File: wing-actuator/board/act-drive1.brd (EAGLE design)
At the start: 112.5 x 79.2 mm, 137 parts, among them J1 POWER_JACKPTH_LOCK, Q1 BSS123, Q2 BSS123, Q3 BSS123, Q4 BSS123, Q5 BSS123, Q6 BSS123, T1 ATB3225, U1 LT3468-1, X1 SMA-142-0701-801/806, X2 SMA-142-0701-801/806, X3 SMA-142-0701-801/806, X4 SMA-142-0701-801/806, X5 2516-, X6 2516-, X7 SSW-102-02-S-D

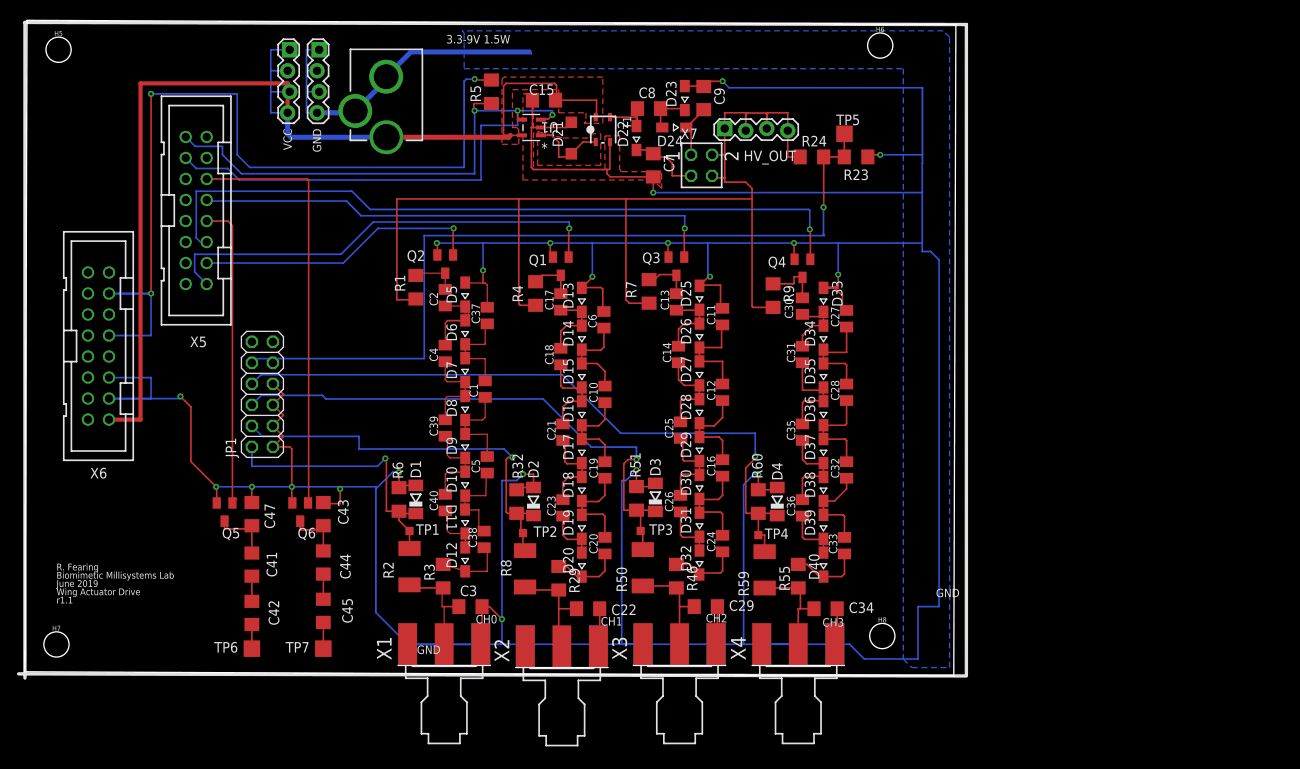
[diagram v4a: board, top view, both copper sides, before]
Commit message: done routing. need to add attributes for BoM
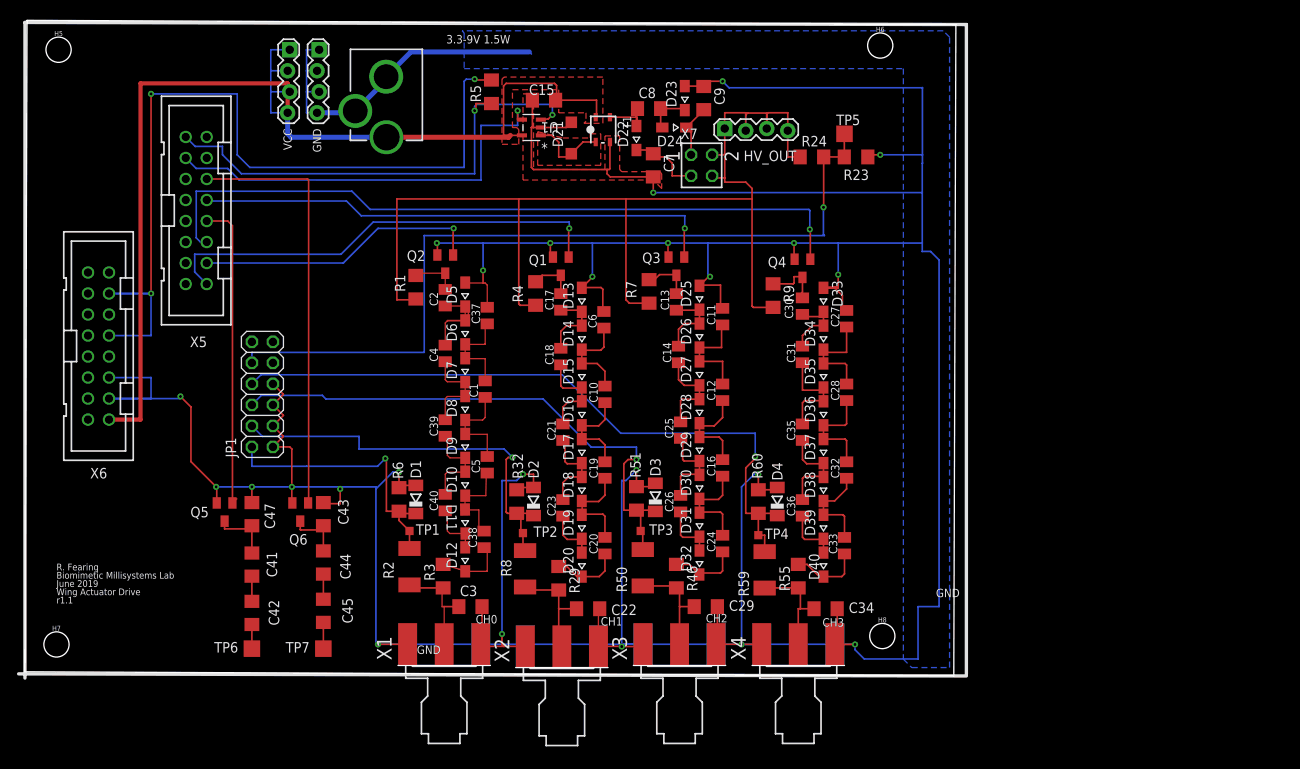
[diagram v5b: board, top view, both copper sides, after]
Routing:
- net GND: track 617.0 -> 639.0 mm, vias 21 -> 25
- net DONE*: track 59.5 -> 60.7 mm

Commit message: renumbered parts
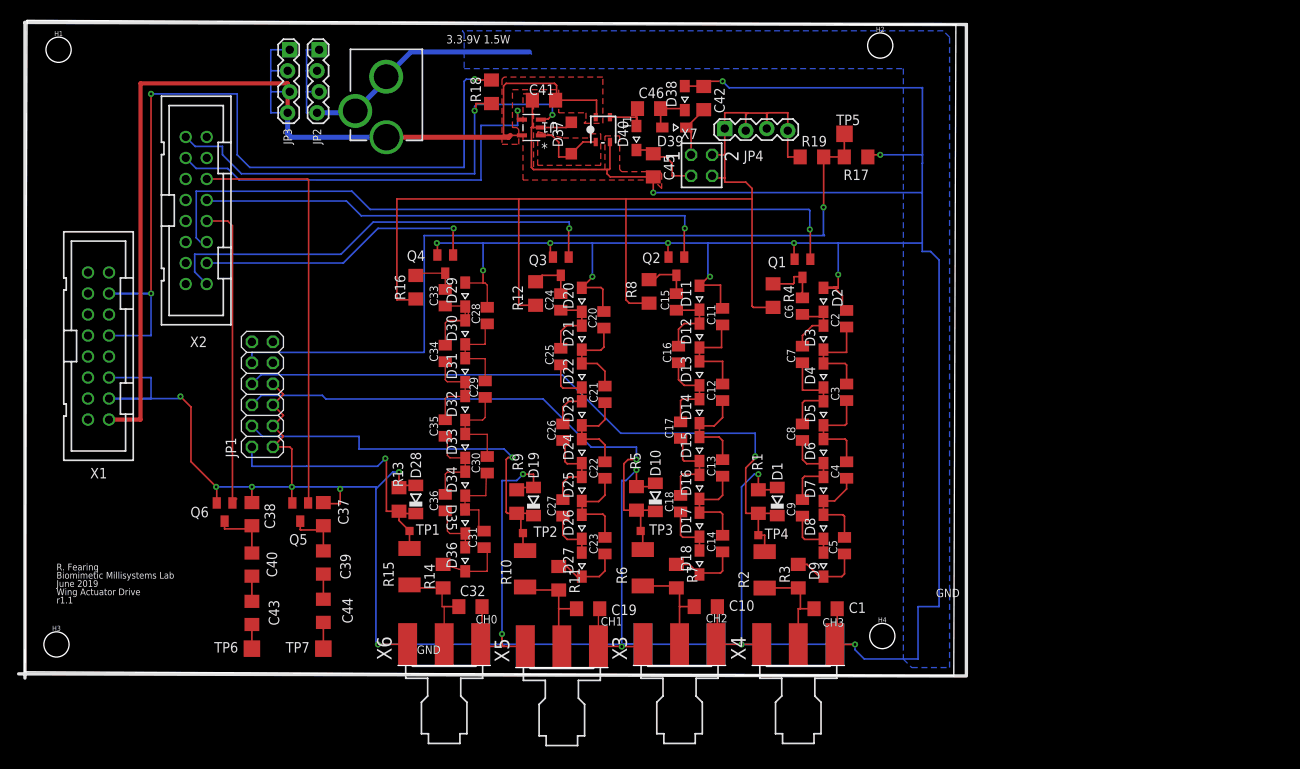
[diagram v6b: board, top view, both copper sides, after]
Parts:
- removed C47: 220 pF, 1000V, rcl:C1206
- removed R32, R60: 22k, rcl:R1206
- removed R46, R55: 1M, rcl:R1206
- removed R50, R59: 10M, rcl:R2010
- removed R51: 22K, rcl:R1206
- added C46: 0.1uF 450V, rcl:C1206
- added R10, R15: 10M, rcl:R2010
- added R12, R16: 10M, rcl:R1206
- added R13: 22k, rcl:R1206
- added R14: 1M, rcl:R1206
- added R18: 100K, resistor:R1206
- C1, C10, C19: value 3.3nF -> 1nF 1k5V; device rcl:C0805K -> rcl:C1206
- C15: value 4.7uF -> 3.3nF; device rcl:C1206 -> rcl:C0805K
- C22, C29, C34: value 1nF 1k5V -> 3.3nF; device rcl:C1206 -> rcl:C0805K
- C3: value 1nF-1k5V -> 3.3nF; device rcl:C1206 -> rcl:C0805K
- C32: value 3.3nF -> 1nF-1k5V; device rcl:C0805K -> rcl:C1206
- C37, C38, C39, C40: value 3.3nF -> 220 pF, 1000V; device rcl:C0805K -> rcl:C1206
- C41: value 220 pF, 1000V -> 4.7uF
- C42, C45: value 220 pF, 1000V -> 0.1uF 450V
- C7, C8, C9: value 0.1uF 450V -> 3.3nF; device rcl:C1206 -> rcl:C0805K
- D10, D19, D28: value (none) -> 3.0V; device diode:SOD323-W -> diode:SOD80C
- D2, D3, D4: value 3.0V -> (none); device diode:SOD80C -> diode:SOD323-W
- D21: value B0540W -> (none); device diode:SOD123 -> diode:SOD323-W
- D37: value (none) -> B0540W; device diode:SOD323-W -> diode:SOD123
- R1, R9: value 10M -> 22k
- R5: value 100K -> 22K; device resistor:R1206 -> rcl:R1206
- R6: value 22k -> 10M; device rcl:R1206 -> rcl:R2010
- R7: value 10M -> 1M
- R8: device rcl:R2010 -> rcl:R1206
- T1: device lt3468-1:XFMR3225 -> ActuatorDrive:XFMR3225
- X1, X2: value SMA-142-0701-801/806 -> 2516-; device con-coax:J502-ND-142-0701-801/806 -> con-3m:PAK100/2500-16
- X5, X6: value 2516- -> SMA-142-0701-801/806; device con-3m:PAK100/2500-16 -> con-coax:J502-ND-142-0701-801/806
- moved C42 82.8 mm to (81.8, 69.3), turned to 270 degrees
- moved X2 70.7 mm to (20.4, 55.8), turned to 270 degrees
- moved X5 70.7 mm to (64.6, 0.51), turned to 90 degrees
- moved C45 67.0 mm to (75.7, 61.2), turned to 270 degrees
- moved C41 66.3 mm to (62.5, 69.1), turned to 180 degrees
- moved X1 56.9 mm to (8.64, 39.4), turned to 270 degrees
- moved X6 56.9 mm to (50.4, 0.76), turned to 90 degrees
- moved C33 56.8 mm to (50.5, 45.2)
- moved D40 56.3 mm to (73.7, 64.5)
- moved C34 55.4 mm to (50.5, 38.5), turned to 90 degrees
- moved C3 52.3 mm to (99.1, 33.8), turned to 90 degrees
- moved R5 52.2 mm to (73.7, 21.0), turned to 270 degrees
- moved D39 51.5 mm to (78.2, 65.8), turned to 180 degrees
- moved C9 50.9 mm to (93.7, 19.8), turned to 90 degrees
- moved C4 50.5 mm to (99.1, 24.4)
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- renumbered GND to JP2, H5 to H1, H6 to H2, H7 to H3, H8 to H4, HV_OUT to JP4, R23 to R17, R24 to R19, R29 to R11, U$18 to I1, VCC to JP3
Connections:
- net +3V3: now also R18.2, X1.4, X1.8; no longer R5.2, X6.4, X6.8
- net BOOST: now also C46.2, D38.C, D39.A; no longer C8.2, D23.C, D24.A
- net BOOST1: now also C45.1, D40.C; no longer C7.1, D22.C
- net BOOST2: now also C42.2, D39.C; no longer C9.2, D24.C
- net DONE*: now also R18.1, X2.1; no longer R5.1, X5.1
- net GND: now also C1.2, C10.2, C19.2, C2.2, C20.2, C28.2, C32.2, C38.2, C41.2, C42.1, C45.2, D10.A, D11.A, D19.A, D20.A, D28.A, D29.A, D37.A, D38.A, R1.1, R13.1, R5.1, R9.1, X1.12, X1.14, X5.G@1, X5.G@2, X5.G@3, X5.G@4, X6.G@1, X6.G@2, X6.G@3, X6.G@4; no longer C15.2, C22.2, C27.2, C29.2, C3.2, C34.2, C43.2, C47.2, C6.2, C7.2, C9.1, D13.A, D21.A, D23.A, D25.A, D3.A, D33.A, D4.A, D5.A, R32.1, R51.1, R6.1, R60.1, X1.G@1, X1.G@2, X1.G@3, X1.G@4, X2.G@1, X2.G@2, X2.G@3, X2.G@4, X6.12, X6.14
- net N$1: now also C29.1, C30.2, D32.C, D33.A; no longer C1.1, C5.2, D8.C, D9.A
- net N$10: now also C35.1, C36.2, D33.C, D34.A; no longer C39.1, C40.2, D10.A, D9.C
- net N$11: now also C24.1, C25.2, D20.C, D21.A; no longer C17.1, C18.2, D13.C, D14.A
- net N$12: now also D37.C; no longer D21.C
- net N$13: now also C20.1, C21.2, D21.C, D22.A; no longer C10.2, C6.1, D14.C, D15.A
- net N$14: now also C27.1, D26.C, D27.A; no longer C23.1, D19.C, D20.A
- net N$15: now also C21.1, C22.2, D23.C, D24.A; no longer C10.1, C19.2, D16.C, D17.A
- net N$16: now also C22.1, C23.2, D25.C, D26.A; no longer C19.1, C20.2, D18.C, D19.A
- net N$17: now also C15.1, C16.2, D11.C, D12.A; no longer C13.1, C14.2, D25.C, D26.A
- net N$18: now also D12.C, D13.A; no longer D26.C, D27.A
- net N$2: now also C33.1, C34.2, D29.C, D30.A; no longer C2.1, C4.2, D5.C, D6.A
- net N$20: now also C18.1, D17.C, D18.A; no longer C26.1, D31.C, D32.A
- net N$21: now also C25.1, C26.2, D22.C, D23.A; no longer C18.1, C21.2, D15.C, D16.A
- net N$22: now also C26.1, C27.2, D24.C, D25.A; no longer C21.1, C23.2, D17.C, D18.A
- net N$23: now also C24.2, Q3.3, R12.1; no longer C17.2, Q1.3, R4.1
- net N$24: now also C13.2, D14.C, D15.A; no longer C16.2, D28.C, D29.A
- net N$25: now also C13.1, C14.2, D16.C, D17.A; no longer C16.1, C24.2, D30.C, D31.A
- net N$26: now also C5.1, D9.C, R3.1; no longer C33.1, D40.C, R55.1
- net N$27: now also C16.1, C17.2, D13.C, D14.A; no longer C14.1, C25.2, D27.C, D28.A
- net N$29: now also C17.1, C18.2, D15.C, D16.A; no longer C25.1, C26.2, D29.C, D30.A
- net N$3: now also C31.1, D36.C, R14.1; no longer C38.1, D12.C, R3.1
- net N$30: now also C15.2, Q2.3, R8.1; no longer C13.2, Q3.3, R7.1
- net N$32: now also C6.1, C7.2, D2.C, D3.A; no longer C30.1, C31.2, D33.C, D34.A
- net N$33: now also C2.1, C3.2, D3.C, D4.A; no longer C27.1, C28.2, D34.C, D35.A
- net N$34: now also C9.1, D8.C, D9.A; no longer C36.1, D39.C, D40.A
- net N$35: now also C3.1, C4.2, D5.C, D6.A; no longer C28.1, C32.2, D36.C, D37.A
- net N$36: now also C4.1, C5.2, D7.C, D8.A; no longer C32.1, C33.2, D38.C, D39.A
- net N$37: now also C7.1, C8.2, D4.C, D5.A; no longer C31.1, C35.2, D35.C, D36.A
- net N$38: now also C8.1, C9.2, D6.C, D7.A; no longer C35.1, C36.2, D37.C, D38.A
- net N$39: now also C6.2, Q1.3, R4.1; no longer C30.2, Q4.3, R9.1
- net N$4: now also C14.1, D18.C, R7.1; no longer C24.1, D32.C, R46.1
- net N$40: now also C43.1; no longer C42.1
- net N$41: now also C40.1, C43.2; no longer C41.1, C42.2
- net N$42: now also C38.1, C40.2, Q6.3; no longer C41.2, C47.1, Q5.3
- net N$43: now also C44.1; no longer C45.1
- net N$44: now also C39.1, C44.2; no longer C44.1, C45.2
- net N$45: now also C37.1, C39.2, Q5.3; no longer C43.1, C44.2, Q6.3
- net N$5: now also C28.1, C29.2, D30.C, D31.A; no longer C1.2, C37.1, D6.C, D7.A
- net N$59: now also C36.1, D35.C, D36.A; no longer C40.1, D11.C, D12.A
- net N$6: now also C46.1, D40.A; no longer C8.1, D22.A
- net N$61: now also C30.1, C31.2, D34.C, D35.A; no longer C38.2, C5.1, D10.C, D11.A
- net N$7: now also C34.1, C35.2, D31.C, D32.A; no longer C39.2, C4.1, D7.C, D8.A
- net N$8: now also C33.2, Q4.3, R16.1; no longer C2.2, Q2.3, R1.1
- net N$9: now also C23.1, D27.C; no longer C20.1, D20.C
- net PWM_0: now also Q4.1, X2.14; no longer Q2.1, X5.14
- net PWM_1: now also Q3.1, X2.16; no longer Q1.1, X5.16
- net PWM_2: now also Q2.1, X2.8; no longer Q3.1, X5.8
- net PWM_3: now also Q1.1, X2.12; no longer Q4.1, X5.12
- net SD_2: now also Q6.1, X2.10; no longer Q5.1, X5.10
- net SD_3: now also Q5.1, X2.6; no longer Q6.1, X5.6
- net START: now also X2.3; no longer X5.3
- net V+: now also R12.2, R16.2, R8.2; no longer R1.2, R7.2, R9.2
- net VCC: now also C41.1, X1.16; no longer C15.1, X6.16
- net VO0: now also C32.1, R14.2, R15.2, X6.1; no longer C3.1, R2.2, R3.2, X1.1
- net VO1: now also C19.1, R10.2, X5.1; no longer C22.1, R8.2, X2.1
- net VO2: now also C10.1, R6.2, R7.2; no longer C29.1, R46.2, R50.2
- net VO3: now also C1.1, R2.2, R3.2; no longer C34.1, R55.2, R59.2
- net V_SENSE0: now also D28.C, R13.2, R15.1; no longer D1.C, R2.1, R6.2
- net V_SENSE1: now also D19.C, R10.1, R9.2; no longer D2.C, R32.2, R8.1
- net V_SENSE2: now also D10.C, R5.2, R6.1; no longer D3.C, R50.1, R51.2
- net V_SENSE3: now also D1.C, R1.2, R2.1; no longer D4.C, R59.1, R60.2

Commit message: added digikey part #s
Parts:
- removed X1, X2: 2516-, con-3m:PAK100/2500-16
- added D41: 3.0V, diode:SOD80C
- added SV1, SV2: (no value), con-harting-ml:ML16
- C32: value 1nF-1k5V -> 1nF 1k5V
- R11, R14, R3, R7: value 1M -> 1.0M
- R12, R16, R4, R8: value 10M -> 1.0M
- R18: value 100K -> 22K
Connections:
- net +3V3: now also SV1.4, SV1.8; no longer X1.4, X1.8
- net DONE*: now also SV2.1; no longer X2.1
- net GND: now also D41.A, SV1.12, SV1.14; no longer X1.12, X1.14
- net HV_SENSE: now also D41.C
- net PWM_0: now also SV2.14; no longer X2.14
- net PWM_1: now also SV2.16; no longer X2.16
- net PWM_2: now also SV2.8; no longer X2.8
- net PWM_3: now also SV2.12; no longer X2.12
- net SD_2: now also SV2.10; no longer X2.10
- net SD_3: now also SV2.6; no longer X2.6
- net START: now also SV2.3; no longer X2.3
- net VCC: now also SV1.16; no longer X1.16
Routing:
- net +3V3: track 104.2 -> 99.6 mm
- net HV_SENSE: track 99.4 -> 102.9 mm
- net GND: track 639.0 -> 640.6 mm
- net VCC: track 135.5 -> 137.0 mm
- net PWM_2: track 63.6 -> 64.4 mm
- net PWM_0: track 34.9 -> 35.6 mm
- net START: track 51.2 -> 52.0 mm
- net SD_3: track 51.4 -> 52.2 mm
- net SD_2: track 37.6 -> 38.3 mm
- net DONE*: track 60.7 -> 61.5 mm
- net PWM_3: track 88.4 -> 89.1 mm

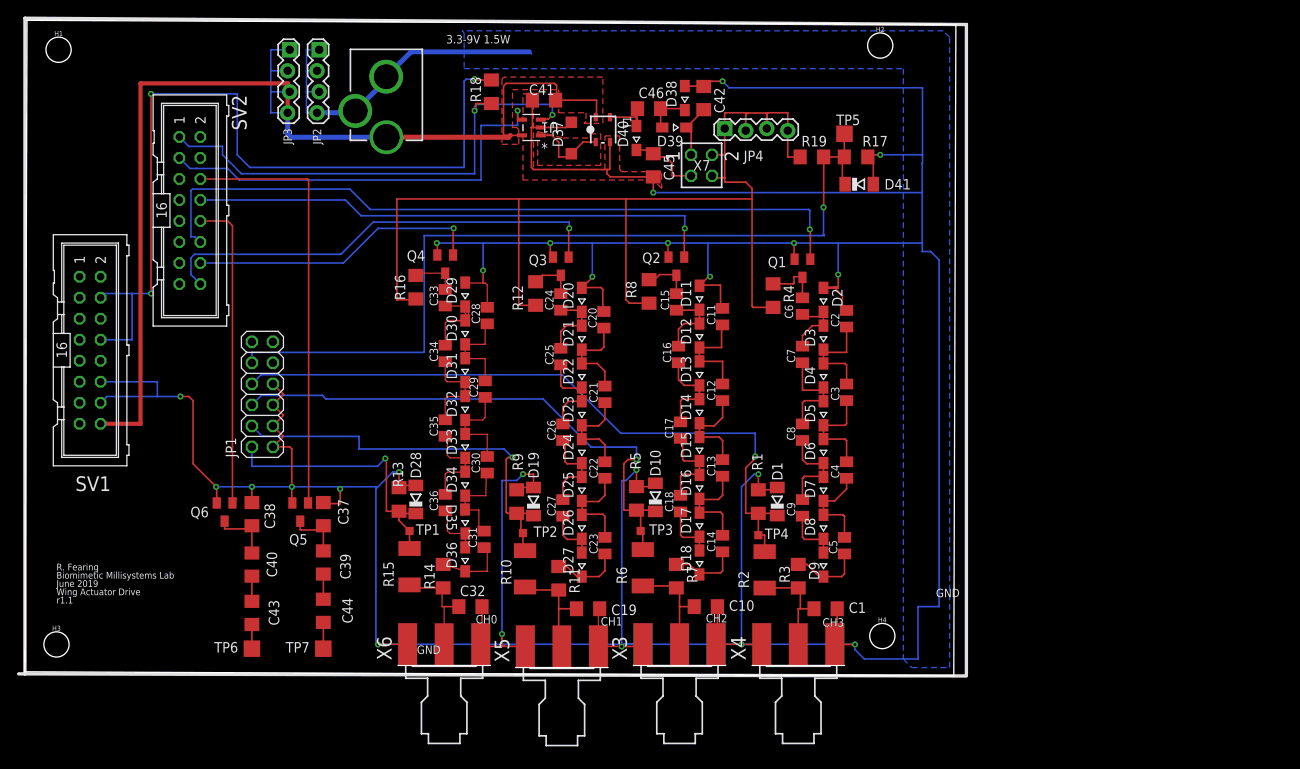
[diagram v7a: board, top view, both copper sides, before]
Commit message: changed all lines to 8 mil min width
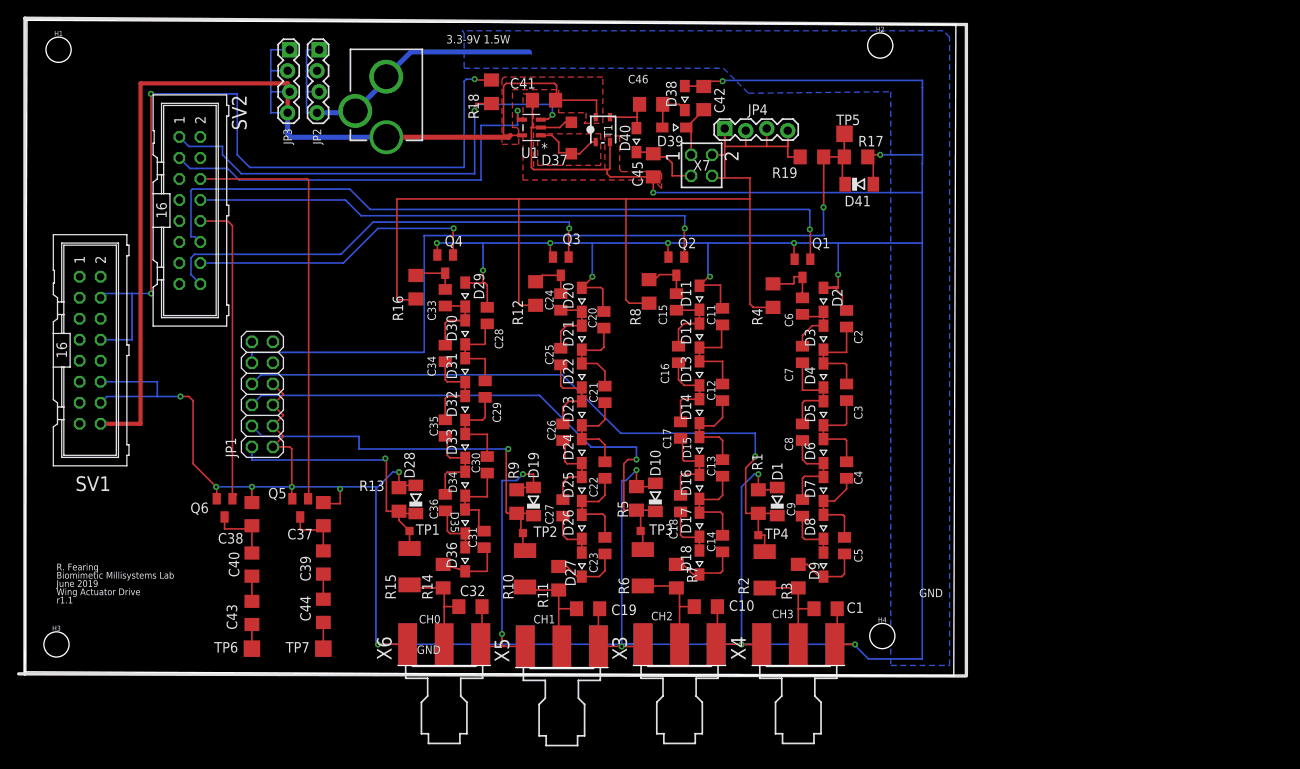
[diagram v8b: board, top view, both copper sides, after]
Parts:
- C1, C10, C19, C32: value 1nF 1k5V -> 1nF
- C37, C38, C39, C40, C43, C44: value 220 pF, 1000V -> 220 pF
- C42, C45, C46: value 0.1uF 450V -> 0.1uF
- moved C46 0.57 mm to (75.4, 68.6)
- moved Q5 0.51 mm to (33.0, 19.8)
- moved Q6 0.51 mm to (23.9, 19.8)
- moved D40 0.25 mm to (73.7, 64.3)
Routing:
- net GND: track 640.6 -> 636.4 mm
- net V+: track 143.5 -> 139.5 mm
- net N$2: track 13.8 -> 11.6 mm
- net V_SENSE0: track 34.1 -> 33.0 mm
- net N$12: track 9.50 -> 8.88 mm
- net SD_3: track 52.2 -> 51.7 mm
- net N$45: track 7.17 -> 7.67 mm
- net N$42: track 7.69 -> 8.19 mm
- net SD_2: track 38.3 -> 37.8 mm
